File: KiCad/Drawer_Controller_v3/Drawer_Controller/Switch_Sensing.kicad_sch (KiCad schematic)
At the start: 4 parts, among them U9 SMF05CT1G

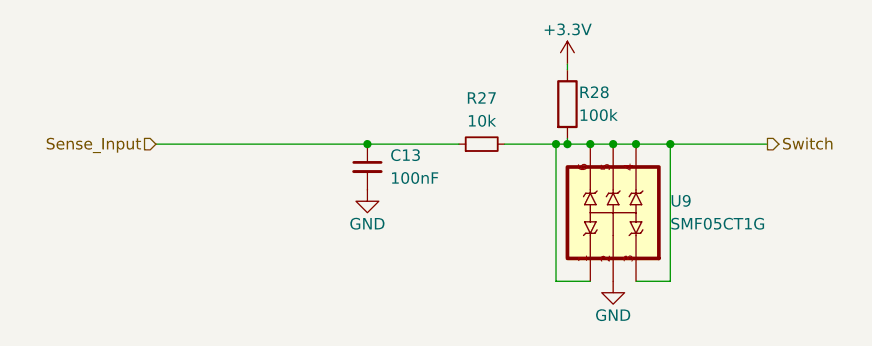
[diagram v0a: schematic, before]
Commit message: Progress in updating schematic for v3 - WIP
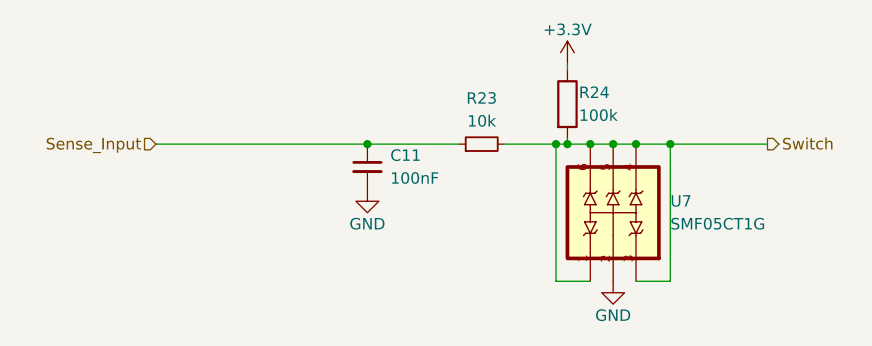
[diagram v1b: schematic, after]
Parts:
- renumbered C13 to C11, R27 to R23, R28 to R24, U9 to U7

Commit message: Adding the power stage, but still WIP
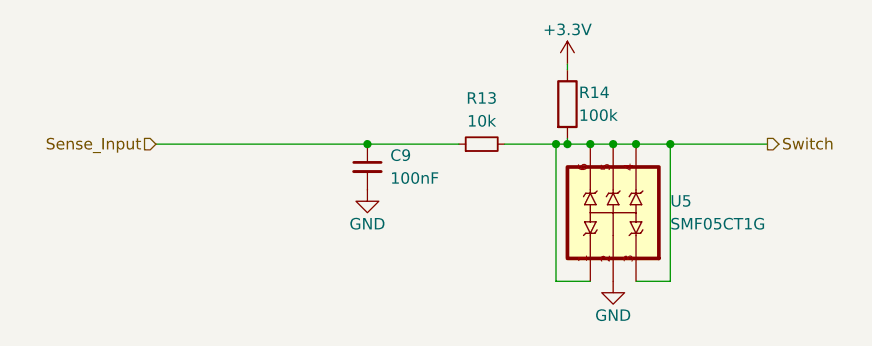
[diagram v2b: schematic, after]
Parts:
- renumbered C11 to C9, R23 to R13, R24 to R14, U7 to U5
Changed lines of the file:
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@@
   (symbol (lib_id "power:GND") (at 109.855 90.17 0) (unit 1)
     (in_bom yes) (on_board yes) (dnp no)
-    (property "Reference" "#PWR0144" (at 109.855 96.52 0)
+    (property "Reference" "#PWR032" (at 109.855 96.52 0)
       (effects (font (size 1.27 1.27)) hide)
     )
@@
   (symbol (lib_id "power:GND") (at 137.16 100.33 0) (unit 1)
     (in_bom yes) (on_board yes) (dnp no)
-    (property "Reference" "#PWR0143" (at 137.16 106.68 0)
+    (property "Reference" "#PWR034" (at 137.16 106.68 0)
       (effects (font (size 1.27 1.27)) hide)
     )
@@
   (symbol (lib_id "SMF05CT1G:SMF05CT1G") (at 137.16 92.71 90) (unit 1)
     (in_bom yes) (on_board yes) (dnp no) (fields_autoplaced)
-    (property "Reference" "U7" (at 143.51 91.4399 90)
+    (property "Reference" "U5" (at 143.51 91.4399 90)
       (effects (font (size 1.27 1.27)) (justify right))
     )
@@
   (symbol (lib_id "power:+3.3V") (at 132.08 76.2 0) (unit 1)
     (in_bom yes) (on_board yes) (dnp no)
-    (property "Reference" "#PWR0142" (at 132.08 80.01 0)
+    (property "Reference" "#PWR033" (at 132.08 80.01 0)
       (effects (font (size 1.27 1.27)) hide)
     )
@@
   (symbol (lib_id "Device:R") (at 132.08 80.645 0) (unit 1)
     (in_bom yes) (on_board yes) (dnp no)
-    (property "Reference" "R24" (at 133.35 79.375 0)
+    (property "Reference" "R14" (at 133.35 79.375 0)
       (effects (font (size 1.27 1.27)) (justify left))
     )
@@
   (symbol (lib_id "Device:C_Small") (at 109.855 87.63 0) (unit 1)
     (in_bom yes) (on_board yes) (dnp no)
-    (property "Reference" "C11" (at 112.395 86.36 0)
+    (property "Reference" "C9" (at 112.395 86.36 0)
       (effects (font (size 1.27 1.27)) (justify left))
     )
@@
   (symbol (lib_id "Device:R_Small") (at 122.555 85.09 90) (unit 1)
     (in_bom yes) (on_board yes) (dnp no)
-    (property "Reference" "R23" (at 122.555 80.01 90)
-      (effects (font (size 1.27 1.27)))
-    )
+    (property "Reference" "R13" (at 122.555 80.01 90)
+      (effects (font (size 1.27 1.27)))
+    )

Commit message: Starting to connect all the inputs and outputs to the GPIOs of the uC
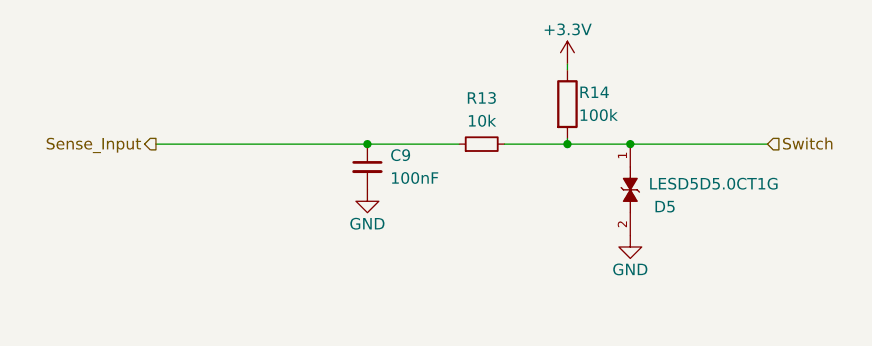
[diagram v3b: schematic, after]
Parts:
- removed U5: SMF05CT1G, SMF05CT1G:SOT65P210X110-6N, symbol SMF05CT1G:SMF05CT1G
- added D5: LESD5D5.0CT1G, TVS_LESD5D5.0CT1G, symbol LESD5D5.0CT1G:LESD5D5.0CT1G
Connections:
- net GND: now also D5.2
- net Switch: now also D5.1

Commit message: Finished first draft for connecting all GPIOs
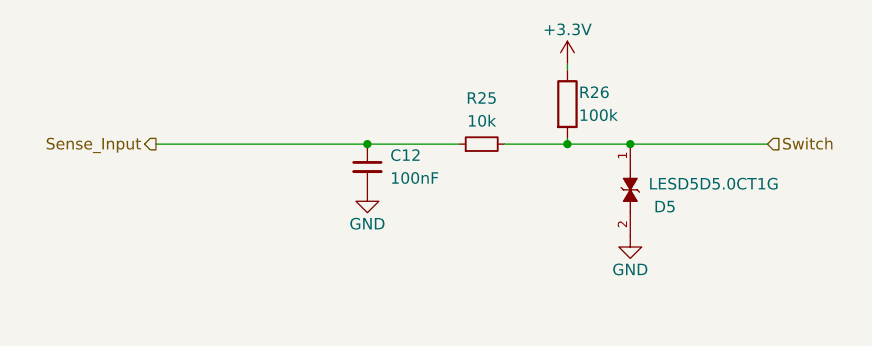
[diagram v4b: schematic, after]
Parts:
- renumbered C9 to C12, R13 to R25, R14 to R26
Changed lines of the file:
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@@
   (symbol (lib_id "power:GND") (at 109.855 90.17 0) (unit 1)
     (in_bom yes) (on_board yes) (dnp no)
-    (property "Reference" "#PWR032" (at 109.855 96.52 0)
+    (property "Reference" "#PWR048" (at 109.855 96.52 0)
       (effects (font (size 1.27 1.27)) hide)
     )
@@
   (symbol (lib_id "power:GND") (at 139.065 95.25 0) (unit 1)
     (in_bom yes) (on_board yes) (dnp no)
-    (property "Reference" "#PWR034" (at 139.065 101.6 0)
+    (property "Reference" "#PWR050" (at 139.065 101.6 0)
       (effects (font (size 1.27 1.27)) hide)
     )
@@
   (symbol (lib_id "power:+3.3V") (at 132.08 76.2 0) (unit 1)
     (in_bom yes) (on_board yes) (dnp no)
-    (property "Reference" "#PWR033" (at 132.08 80.01 0)
+    (property "Reference" "#PWR049" (at 132.08 80.01 0)
       (effects (font (size 1.27 1.27)) hide)
     )
@@
   (symbol (lib_id "Device:R") (at 132.08 80.645 0) (unit 1)
     (in_bom yes) (on_board yes) (dnp no)
-    (property "Reference" "R14" (at 133.35 79.375 0)
+    (property "Reference" "R26" (at 133.35 79.375 0)
       (effects (font (size 1.27 1.27)) (justify left))
     )
@@
   (symbol (lib_id "Device:C_Small") (at 109.855 87.63 0) (unit 1)
     (in_bom yes) (on_board yes) (dnp no)
-    (property "Reference" "C9" (at 112.395 86.36 0)
+    (property "Reference" "C12" (at 112.395 86.36 0)
       (effects (font (size 1.27 1.27)) (justify left))
     )
@@
   (symbol (lib_id "Device:R_Small") (at 122.555 85.09 90) (unit 1)
     (in_bom yes) (on_board yes) (dnp no)
-    (property "Reference" "R13" (at 122.555 80.01 90)
-      (effects (font (size 1.27 1.27)))
-    )
+    (property "Reference" "R25" (at 122.555 80.01 90)
+      (effects (font (size 1.27 1.27)))
+    )

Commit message: Finished assigning all footprints
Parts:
- C12: footprint Capacitor_SMD:C_0805_2012Metric_Pad1.18x1.45mm_HandSolder -> Capacitor_SMD:C_0402_1005Metric
- D5: footprint TVS_LESD5D5.0CT1G -> Robast_Footprints:TVS_LESD5D5.0CT1G
- R25, R26: footprint Resistor_SMD:R_0805_2012Metric_Pad1.20x1.40mm_HandSolder -> Capacitor_SMD:C_0603_1608Metric
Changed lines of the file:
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@@
       (effects (font (size 1.27 1.27)) (justify left))
     )
-    (property "Footprint" "Resistor_SMD:R_0805_2012Metric_Pad1.20x1.40mm_HandSolder" (at 130.302 80.645 90)
+    (property "Footprint" "Capacitor_SMD:C_0603_1608Metric" (at 130.302 80.645 90)
       (effects (font (size 1.27 1.27)) hide)
     )
@@
       (effects (font (size 1.27 1.27)) (justify left))
     )
-    (property "Footprint" "Capacitor_SMD:C_0805_2012Metric_Pad1.18x1.45mm_HandSolder" (at 109.855 87.63 0)
+    (property "Footprint" "Capacitor_SMD:C_0402_1005Metric" (at 109.855 87.63 0)
       (effects (font (size 1.27 1.27)) hide)
     )
@@
       (effects (font (size 1.27 1.27)) (justify right))
     )
-    (property "Footprint" "TVS_LESD5D5.0CT1G" (at 139.065 90.17 0)
+    (property "Footprint" "Robast_Footprints:TVS_LESD5D5.0CT1G" (at 139.065 90.17 0)
       (effects (font (size 1.27 1.27)) (justify bottom) hide)
     )
@@
       (effects (font (size 1.27 1.27)))
     )
-    (property "Footprint" "Resistor_SMD:R_0805_2012Metric_Pad1.20x1.40mm_HandSolder" (at 122.555 85.09 0)
+    (property "Footprint" "Capacitor_SMD:C_0603_1608Metric" (at 122.555 85.09 0)
       (effects (font (size 1.27 1.27)) hide)
     )

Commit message: Starting routing the PCB - WIP
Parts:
- R25, R26: footprint Capacitor_SMD:C_0603_1608Metric -> Resistor_SMD:R_0402_1005Metric
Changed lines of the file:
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@@
       (effects (font (size 1.27 1.27)) (justify left))
     )
-    (property "Footprint" "Capacitor_SMD:C_0603_1608Metric" (at 130.302 80.645 90)
+    (property "Footprint" "Resistor_SMD:R_0402_1005Metric" (at 130.302 80.645 90)
       (effects (font (size 1.27 1.27)) hide)
     )
@@
       (effects (font (size 1.27 1.27)))
     )
-    (property "Footprint" "Capacitor_SMD:C_0603_1608Metric" (at 122.555 85.09 0)
+    (property "Footprint" "Resistor_SMD:R_0402_1005Metric" (at 122.555 85.09 0)
       (effects (font (size 1.27 1.27)) hide)
     )
